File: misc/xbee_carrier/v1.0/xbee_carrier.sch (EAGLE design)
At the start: 23 parts, among them U2 XBEE-1B3

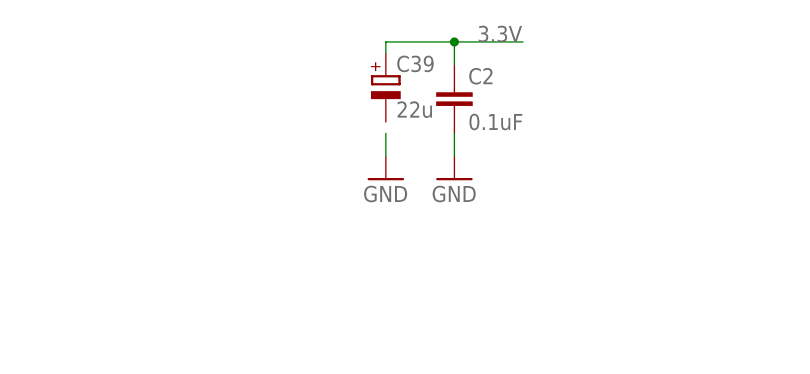
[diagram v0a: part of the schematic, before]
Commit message: Added bom-x attributes and connected the tantalum to ground.
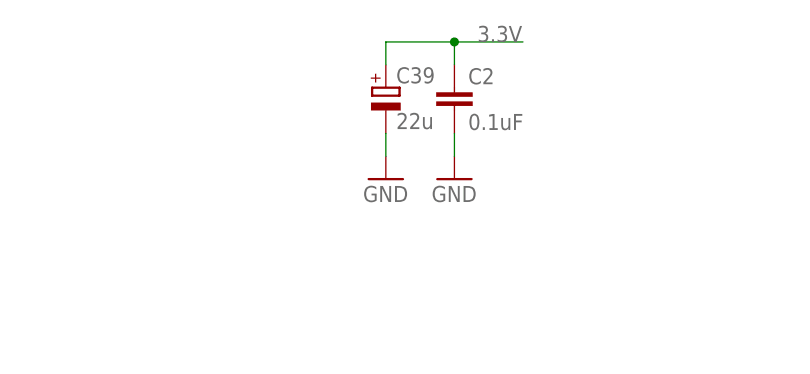
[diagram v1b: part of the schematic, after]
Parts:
- C2: PARTNO (none) -> cap-cer-0402-100n
- C39: PARTNO T491B226M016AT -> cap-tan-B-22u-16v
- JP2, JP3, SJ1, U$1, U$10, U$11, U$16, U$5, U$7, U$9, U2: PARTNO (none) -> *
- LED1, LED2: PARTNO (none) -> led-0402-red
- LED4, LED5: PARTNO (none) -> led-0402-green
- R1, R11, R3, R4: PARTNO (none) -> res-0402-1k5
- X1: PARTNO (none) -> conn-picoblade-smd-0.05in-4
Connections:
- net GND: now also C39.-
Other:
- moved on the sheet: C39
